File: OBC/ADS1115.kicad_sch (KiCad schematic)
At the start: 10 parts, among them J1 Conn_01x10, U4 ADS1115IDGS

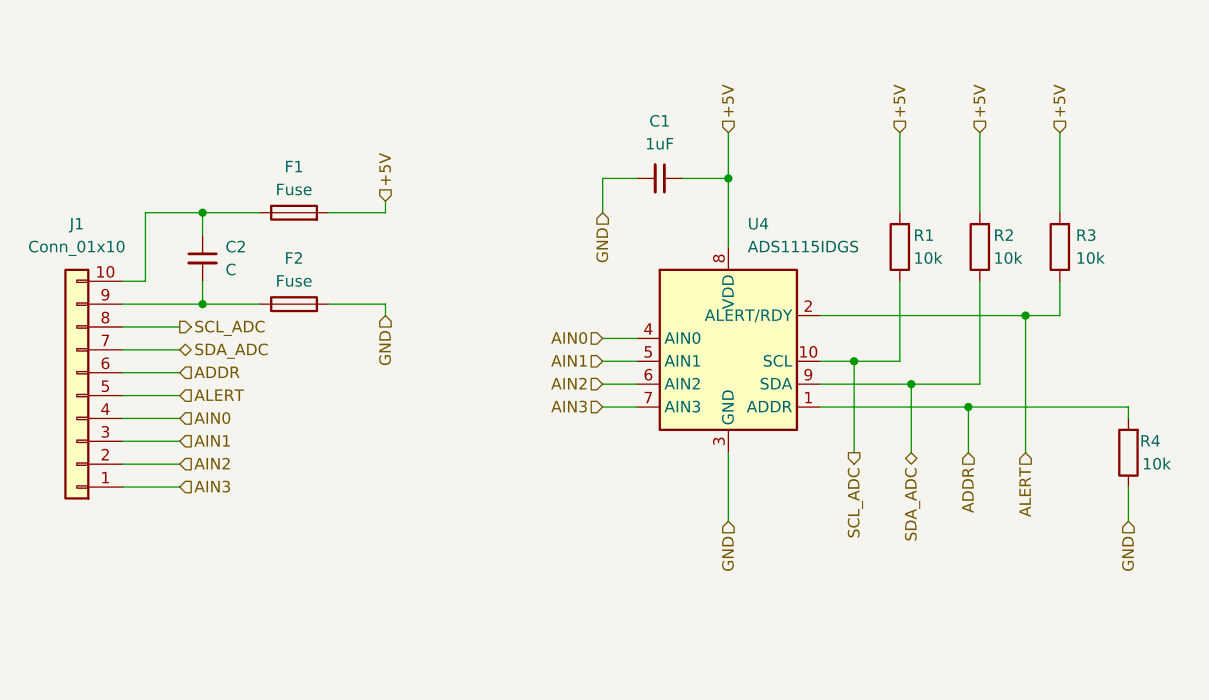
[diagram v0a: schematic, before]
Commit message: Actualiza numeración de componentes
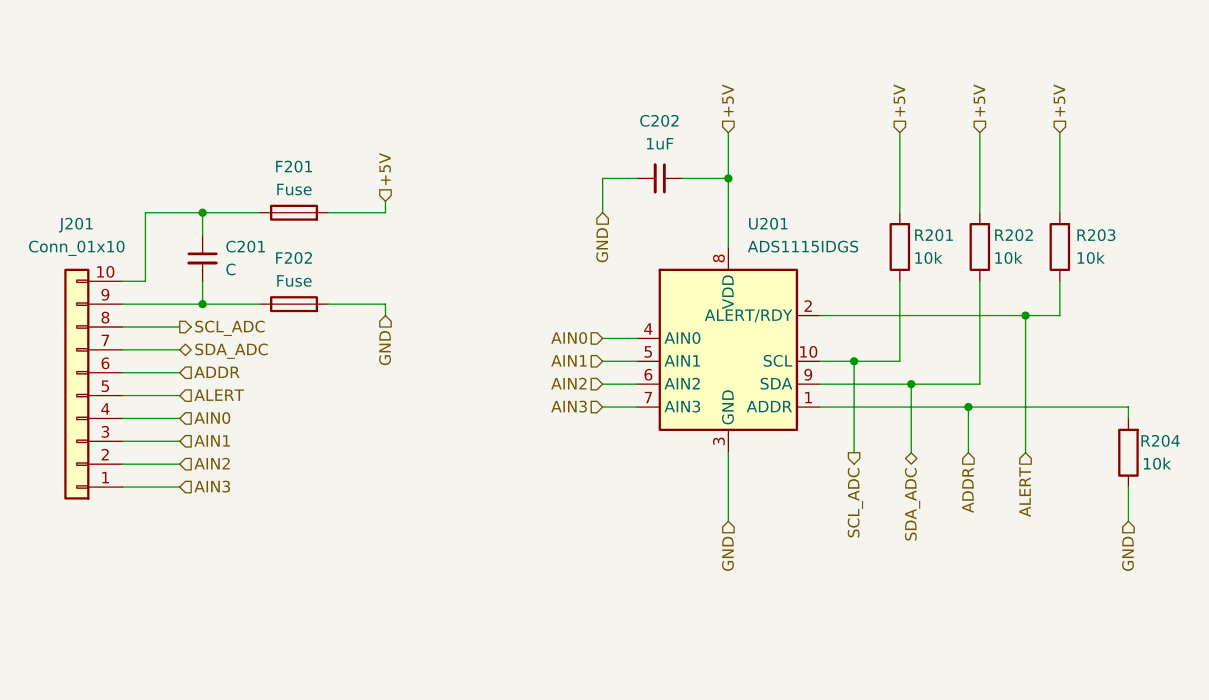
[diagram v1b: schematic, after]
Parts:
- renumbered C2 to C201, C1 to C202, F1 to F201, F2 to F202, J1 to J201, R1 to R201, R2 to R202, R3 to R203, R4 to R204, U4 to U201
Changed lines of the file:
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@@
 		(on_board yes)
 		(dnp no)
-		(property "Reference" "R4"
+		(property "Reference" "R204"
 			(at 209.55 107.95 0)
 			(effects
@@
 			(project "OBC"
 				(path "/1029d1d3-4fe2-46fb-aa7d-396827b97897/60d4d9a8-6d8b-476a-aba6-01999db970ea"
-					(reference "R4")
+					(reference "R204")
 					(unit 1)
 				)
@@
 		(dnp no)
 		(fields_autoplaced yes)
-		(property "Reference" "J1"
+		(property "Reference" "J201"
 			(at 91.44 83.82 0)
 			(effects
@@
 			(project ""
 				(path "/1029d1d3-4fe2-46fb-aa7d-396827b97897/60d4d9a8-6d8b-476a-aba6-01999db970ea"
-					(reference "J1")
+					(reference "J201")
 					(unit 1)
 				)
@@
 		(on_board yes)
 		(dnp no)
-		(property "Reference" "F2"
+		(property "Reference" "F202"
 			(at 115.57 87.63 90)
 			(effects
@@
 			(project "OBC"
 				(path "/1029d1d3-4fe2-46fb-aa7d-396827b97897/60d4d9a8-6d8b-476a-aba6-01999db970ea"
-					(reference "F2")
+					(reference "F202")
 					(unit 1)
 				)
@@
 		(dnp no)
 		(fields_autoplaced yes)
-		(property "Reference" "U4"
+		(property "Reference" "U201"
 			(at 165.9733 83.82 0)
 			(effects
@@
 			(project ""
 				(path "/1029d1d3-4fe2-46fb-aa7d-396827b97897/60d4d9a8-6d8b-476a-aba6-01999db970ea"
-					(reference "U4")
+					(reference "U201")
 					(unit 1)
 				)
@@
 		(dnp no)
 		(fields_autoplaced yes)
-		(property "Reference" "C1"
+		(property "Reference" "C202"
 			(at 156.2036 72.39 90)
 			(effects
@@
 			(project "OBC"
 				(path "/1029d1d3-4fe2-46fb-aa7d-396827b97897/60d4d9a8-6d8b-476a-aba6-01999db970ea"
-					(reference "C1")
+					(reference "C202")
 					(unit 1)
 				)
@@
 		(on_board yes)
 		(dnp no)
-		(property "Reference" "R1"
+		(property "Reference" "R201"
 			(at 184.404 85.09 0)
 			(effects
@@
 			(project ""
 				(path "/1029d1d3-4fe2-46fb-aa7d-396827b97897/60d4d9a8-6d8b-476a-aba6-01999db970ea"
-					(reference "R1")
+					(reference "R201")
 					(unit 1)
 				)
@@
 		(on_board yes)
 		(dnp no)
-		(property "Reference" "R3"
+		(property "Reference" "R203"
 			(at 202.438 85.09 0)
 			(effects
@@
 			(project "OBC"
 				(path "/1029d1d3-4fe2-46fb-aa7d-396827b97897/60d4d9a8-6d8b-476a-aba6-01999db970ea"
-					(reference "R3")
+					(reference "R203")
 					(unit 1)
 				)
@@
 		(on_board yes)
 		(dnp no)
-		(property "Reference" "R2"
+		(property "Reference" "R202"
 			(at 193.294 85.09 0)
 			(effects
@@
 			(project "OBC"
 				(path "/1029d1d3-4fe2-46fb-aa7d-396827b97897/60d4d9a8-6d8b-476a-aba6-01999db970ea"
-					(reference "R2")
+					(reference "R202")
 					(unit 1)
 				)
@@
 		(dnp no)
 		(fields_autoplaced yes)
-		(property "Reference" "C2"
+		(property "Reference" "C201"
 			(at 107.95 86.3662 0)
 			(effects
@@
 			(project ""
 				(path "/1029d1d3-4fe2-46fb-aa7d-396827b97897/60d4d9a8-6d8b-476a-aba6-01999db970ea"
-					(reference "C2")
+					(reference "C201")
 					(unit 1)
 				)
@@
 		(on_board yes)
 		(dnp no)
-		(property "Reference" "F1"
+		(property "Reference" "F201"
 			(at 115.57 77.47 90)
 			(effects
@@
 			(project ""
 				(path "/1029d1d3-4fe2-46fb-aa7d-396827b97897/60d4d9a8-6d8b-476a-aba6-01999db970ea"
-					(reference "F1")
-					(unit 1)
-				)
+					(reference "F201")
+					(unit 1)
+				)

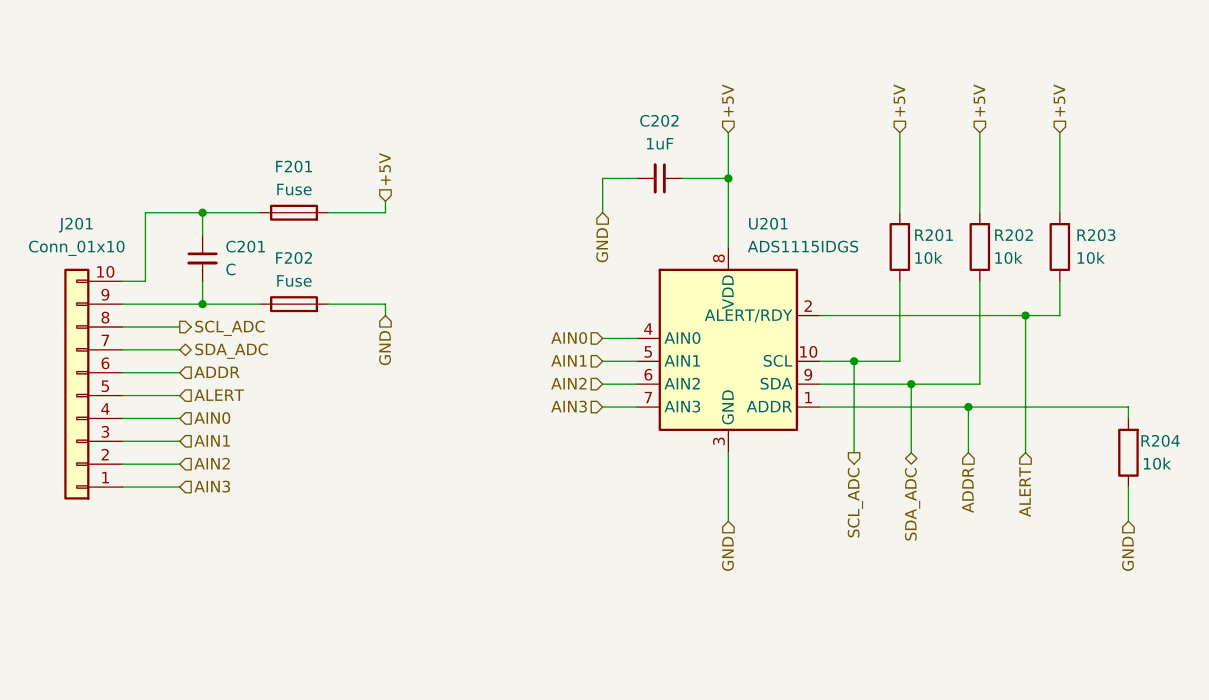
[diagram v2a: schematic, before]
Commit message: Quita conector del sch del ADC
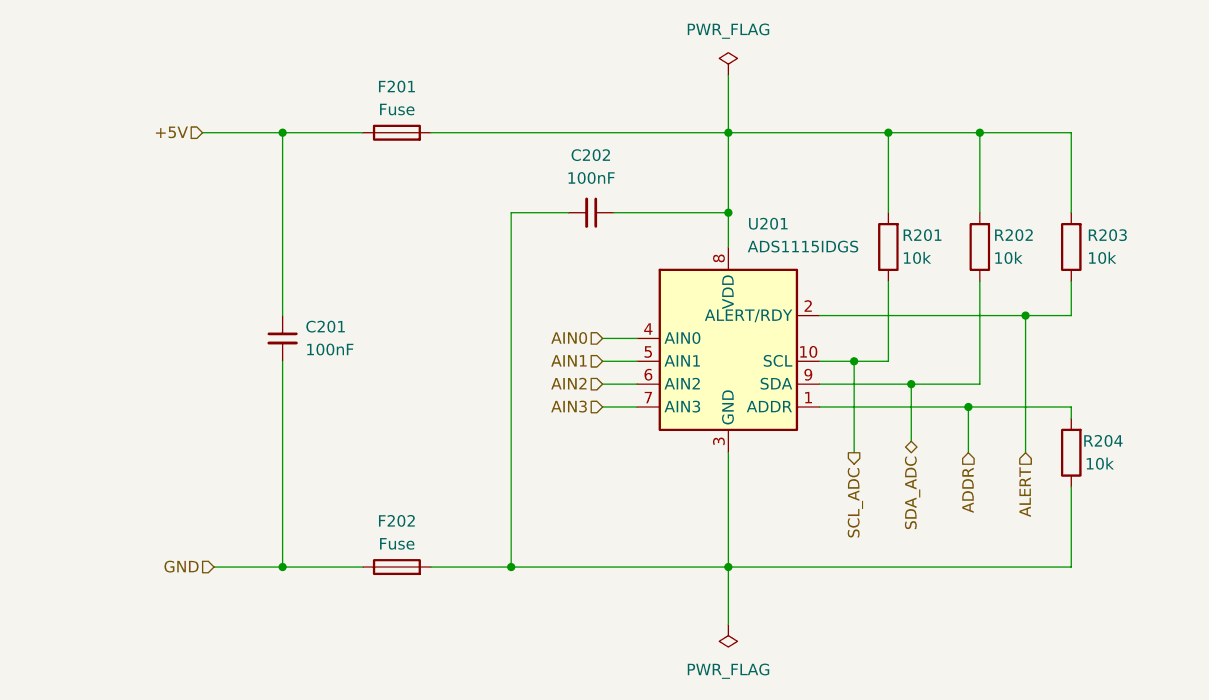
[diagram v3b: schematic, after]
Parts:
- removed J201: Conn_01x10, symbol Connector_Generic:Conn_01x10
- C201: value C -> 100nF; footprint (none) -> Capacitor_SMD:C_0402_1005Metric
- C202: value 1uF -> 100nF; footprint (none) -> Capacitor_SMD:C_0402_1005Metric
- F201, F202: footprint (none) -> Fuse:Fuse_BelFuse_0ZRE0005FF_L8.3mm_W3.8mm
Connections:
- net +5V: now also C201.1, F201.1; no longer C202.1, F201.2, R201.2, R202.2, R203.2, U201.8 (VDD)
- net GND: now also C201.2, F202.1; no longer C202.2, F202.2, R204.1, U201.3 (GND)
- new net: C202.2, F202.2, R204.1, U201.3 (GND)
- new net: C202.1, F201.2, R201.2, R202.2, R203.2, U201.8 (VDD)
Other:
- moved on the sheet: C201, C202, F201, F202, R201, R203, R204

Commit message: Empieza con pcb
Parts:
- F201, F202: footprint Fuse:Fuse_BelFuse_0ZRE0005FF_L8.3mm_W3.8mm -> Fuse:Fuse_0805_2012Metric
- R201, R202, R203, R204: footprint (none) -> Resistor_SMD:R_0603_1608Metric
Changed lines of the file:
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@@
 			)
 		)
-		(property "Footprint" ""
+		(property "Footprint" "Resistor_SMD:R_0603_1608Metric"
 			(at 203.708 109.22 90)
 			(effects
@@
 			)
 		)
-		(property "Footprint" "Fuse:Fuse_BelFuse_0ZRE0005FF_L8.3mm_W3.8mm"
+		(property "Footprint" "Fuse:Fuse_0805_2012Metric"
 			(at 127 123.698 90)
 			(effects
@@
 			)
 		)
-		(property "Footprint" ""
+		(property "Footprint" "Resistor_SMD:R_0603_1608Metric"
 			(at 183.388 86.36 90)
 			(effects
@@
 			)
 		)
-		(property "Footprint" ""
+		(property "Footprint" "Resistor_SMD:R_0603_1608Metric"
 			(at 203.708 86.36 90)
 			(effects
@@
 			)
 		)
-		(property "Footprint" ""
+		(property "Footprint" "Resistor_SMD:R_0603_1608Metric"
 			(at 193.548 86.36 90)
 			(effects
@@
 			)
 		)
-		(property "Footprint" "Fuse:Fuse_BelFuse_0ZRE0005FF_L8.3mm_W3.8mm"
+		(property "Footprint" "Fuse:Fuse_0805_2012Metric"
 			(at 127 75.438 90)
 			(effects

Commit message: Propone disposicion pcb
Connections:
- net +5V renamed +3.3V
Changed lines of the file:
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@@
 		)
 	)
-	(hierarchical_label "+5V"
+	(hierarchical_label "+3.3V"
 		(shape input)
 		(at 105.41 73.66 180)

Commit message: Revisión v1.0
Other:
- company: (none) -> Team Corex
- title: (none) -> Analog-Digital Converter
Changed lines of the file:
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@@
 	(generator_version "9.0")
 	(paper "A4")
+	(title_block
+		(title "Analog-Digital Converter")
+		(date "2025-08-06")
+		(rev "v1.0")
+		(company "Team Corex")
+		(comment 1 "Misión LAMBDA")
+	)
 	(junction
 		(at 139.7 121.92)

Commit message: Correcciones menores
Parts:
- renumbered C202 to C201, C201 to C202
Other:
- company: Team Corex -> Team COREX
- title: Analog-Digital Converter -> OBC - Conversor Analógico-Digital
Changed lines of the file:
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@@
 	(paper "A4")
 	(title_block
-		(title "Analog-Digital Converter")
+		(title "OBC - Conversor Analógico-Digital")
 		(date "2025-08-06")
 		(rev "v1.0")
-		(company "Team Corex")
+		(company "Team COREX")
 		(comment 1 "Misión LAMBDA")
+		(comment 2 "Proyecto CubeSat 2025 UTN")
 	)
 	(junction
@@
 	(wire
 		(pts
-			(xy 163.83 67.31) (xy 163.83 73.66)
-		)
-		(stroke
-			(width 0)
-			(type default)
-		)
-	)
-	(wire
-		(pts
 			(xy 181.61 99.06) (xy 181.61 90.17)
 		)
@@
 		(pts
 			(xy 181.61 73.66) (xy 191.77 73.66)
-		)
-		(stroke
-			(width 0)
-			(type default)
-		)
-	)
-	(wire
-		(pts
-			(xy 163.83 121.92) (xy 163.83 128.27)
 		)
 		(stroke
@@
 				(path "/1029d1d3-4fe2-46fb-aa7d-396827b97897/60d4d9a8-6d8b-476a-aba6-01999db970ea"
 					(reference "R204")
-					(unit 1)
-				)
-			)
-		)
-	)
-	(symbol
-		(lib_id "power:PWR_FLAG")
-		(at 163.83 67.31 0)
-		(unit 1)
-		(exclude_from_sim no)
-		(in_bom yes)
-		(on_board yes)
-		(dnp no)
-		(fields_autoplaced yes)
-		(property "Reference" "#FLG02"
-			(at 163.83 65.405 0)
-			(effects
-				(font
-					(size 1.27 1.27)
-				)
-				(hide yes)
-			)
-		)
-		(property "Value" "PWR_FLAG"
-			(at 163.83 62.23 0)
-			(effects
-				(font
-					(size 1.27 1.27)
-				)
-			)
-		)
-		(property "Footprint" ""
-			(at 163.83 67.31 0)
-			(effects
-				(font
-					(size 1.27 1.27)
-				)
-				(hide yes)
-			)
-		)
-		(property "Datasheet" "~"
-			(at 163.83 67.31 0)
-			(effects
-				(font
-					(size 1.27 1.27)
-				)
-				(hide yes)
-			)
-		)
-		(property "Description" "Special symbol for telling ERC where power comes from"
-			(at 163.83 67.31 0)
-			(effects
-				(font
-					(size 1.27 1.27)
-				)
-				(hide yes)
-			)
-		)
-		(pin "1"
-		)
-		(instances
-			(project "OBC"
-				(path "/1029d1d3-4fe2-46fb-aa7d-396827b97897/60d4d9a8-6d8b-476a-aba6-01999db970ea"
-					(reference "#FLG02")
-					(unit 1)
-				)
-			)
-		)
-	)
-	(symbol
-		(lib_id "power:PWR_FLAG")
-		(at 163.83 128.27 180)
-		(unit 1)
-		(exclude_from_sim no)
-		(in_bom yes)
-		(on_board yes)
-		(dnp no)
-		(fields_autoplaced yes)
-		(property "Reference" "#FLG01"
-			(at 163.83 130.175 0)
-			(effects
-				(font
-					(size 1.27 1.27)
-				)
-				(hide yes)
-			)
-		)
-		(property "Value" "PWR_FLAG"
-			(at 163.83 133.35 0)
-			(effects
-				(font
-					(size 1.27 1.27)
-				)
-			)
-		)
-		(property "Footprint" ""
-			(at 163.83 128.27 0)
-			(effects
-				(font
-					(size 1.27 1.27)
-				)
-				(hide yes)
-			)
-		)
-		(property "Datasheet" "~"
-			(at 163.83 128.27 0)
-			(effects
-				(font
-					(size 1.27 1.27)
-				)
-				(hide yes)
-			)
-		)
-		(property "Description" "Special symbol for telling ERC where power comes from"
-			(at 163.83 128.27 0)
-			(effects
-				(font
-					(size 1.27 1.27)
-				)
-				(hide yes)
-			)
-		)
-		(pin "1"
-		)
-		(instances
-			(project ""
-				(path "/1029d1d3-4fe2-46fb-aa7d-396827b97897/60d4d9a8-6d8b-476a-aba6-01999db970ea"
-					(reference "#FLG01")
 					(unit 1)
 				)
@@
 		(dnp no)
 		(fields_autoplaced yes)
-		(property "Reference" "C202"
+		(property "Reference" "C201"
 			(at 148.5836 76.2 90)
 			(effects
@@
 			(project "OBC"
 				(path "/1029d1d3-4fe2-46fb-aa7d-396827b97897/60d4d9a8-6d8b-476a-aba6-01999db970ea"
-					(reference "C202")
+					(reference "C201")
 					(unit 1)
 				)
@@
 		(dnp no)
 		(fields_autoplaced yes)
-		(property "Reference" "C201"
+		(property "Reference" "C202"
 			(at 116.84 95.2562 0)
 			(effects
@@
 			(project "OBC"
 				(path "/1029d1d3-4fe2-46fb-aa7d-396827b97897/60d4d9a8-6d8b-476a-aba6-01999db970ea"
-					(reference "C201")
+					(reference "C202")
 					(unit 1)
 				)

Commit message: Remueve hmi fisico del obs y renombra componentes
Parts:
- renumbered C202 to C201, C201 to C202
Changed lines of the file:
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@@
 		(dnp no)
 		(fields_autoplaced yes)
-		(property "Reference" "C201"
+		(property "Reference" "C202"
 			(at 148.5836 76.2 90)
 			(effects
@@
 			(project "OBC"
 				(path "/1029d1d3-4fe2-46fb-aa7d-396827b97897/60d4d9a8-6d8b-476a-aba6-01999db970ea"
-					(reference "C201")
+					(reference "C202")
 					(unit 1)
 				)
@@
 		(dnp no)
 		(fields_autoplaced yes)
-		(property "Reference" "C202"
+		(property "Reference" "C201"
 			(at 116.84 95.2562 0)
 			(effects
@@
 			(project "OBC"
 				(path "/1029d1d3-4fe2-46fb-aa7d-396827b97897/60d4d9a8-6d8b-476a-aba6-01999db970ea"
-					(reference "C202")
-					(unit 1)
-				)
+					(reference "C201")
+					(unit 1)
+				)
